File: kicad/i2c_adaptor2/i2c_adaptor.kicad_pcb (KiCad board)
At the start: 2 copper layers, 16 parts, among them J1 Conn_01x02, J2 Conn_01x05, J3 Conn_01x03, J4 Conn_01x14, J5 Conn_01x02, J6 Conn_01x14, Q1 Fairchild BS170, Q2 Fairchild BS170, SW1 SW_SPDT, U1 pic16f18326

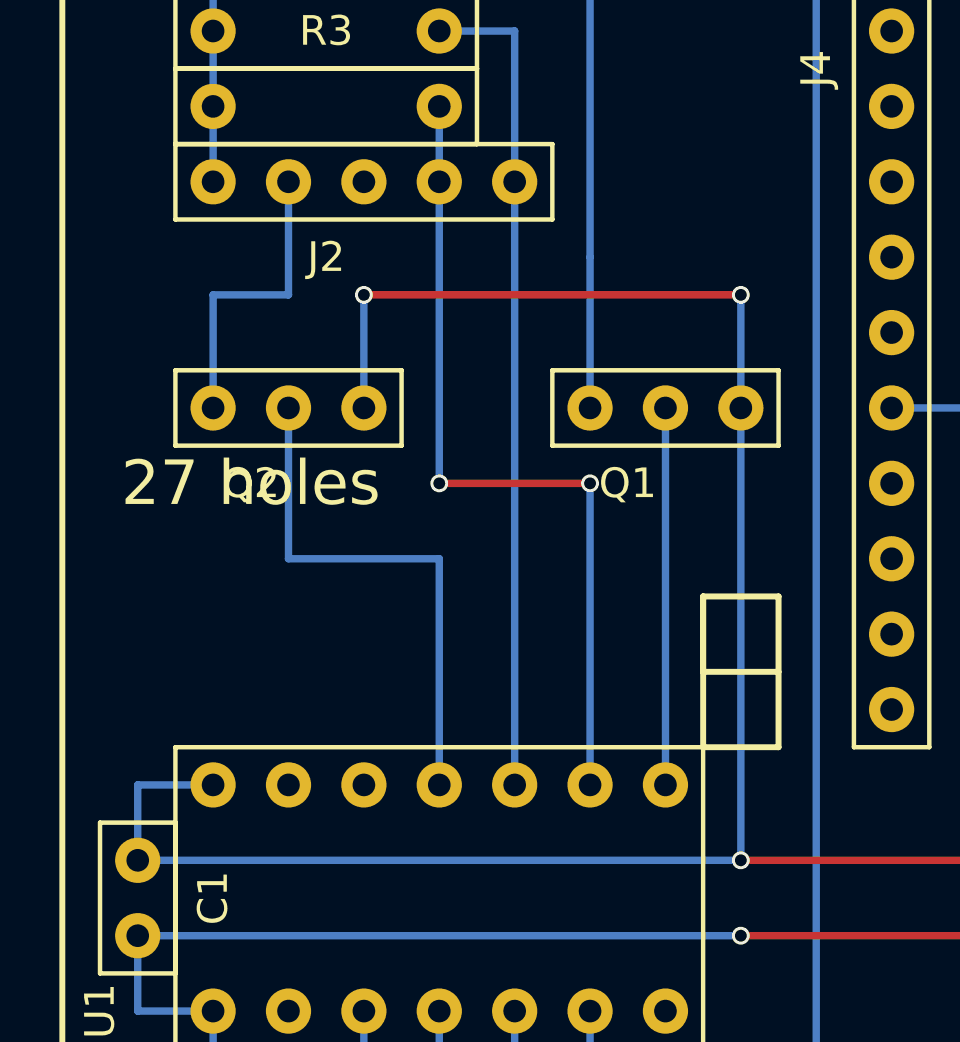
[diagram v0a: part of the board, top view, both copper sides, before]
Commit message: schematic update
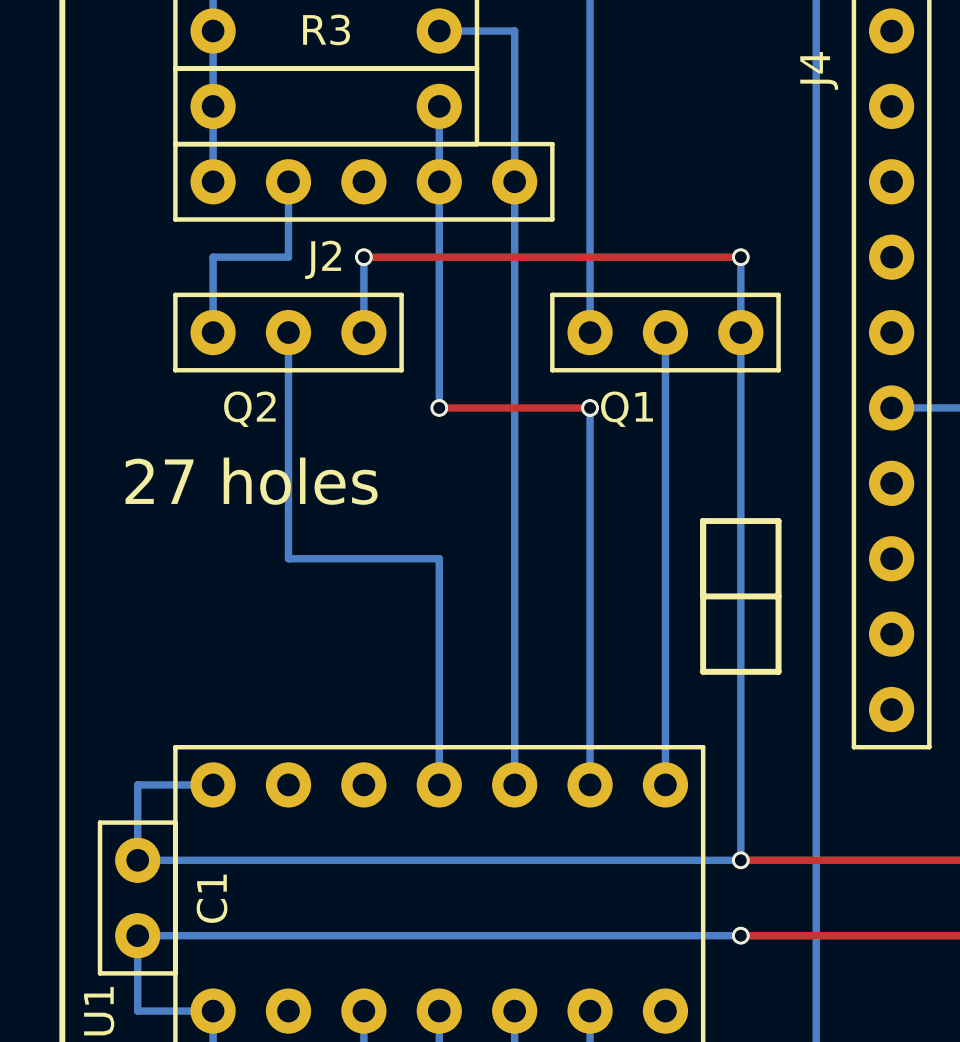
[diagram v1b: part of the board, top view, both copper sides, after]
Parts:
- moved Q1 2.54 mm to (182.9, 102.9)
- moved Q2 2.54 mm to (170.2, 102.9)
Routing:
- net Net-(Q2-Pad2): track 17.8 -> 20.3 mm
- net Net-(Q1-Pad2): track 12.7 -> 15.2 mm
- net FET2: track 10.2 -> 7.62 mm
- net FET1: track 33.0 -> 30.5 mm
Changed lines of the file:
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@@
     (links 34)
     (no_connects 0)
-    (area 0 0 0 0)
+    (area 161.585 72.289999 209.355 144.585)
     (thickness 1.6)
     (drawings 51)
@@
   )
   (module pic16f1:BS170 (layer F.Cu)
-    (at 182.88 105.41)
+    (at 182.88 102.87)
     (fp_text reference Q1 (at -1.27 2.54) (layer F.SilkS)
       (effects (font (size 1 1) (thickness 0.15)))
@@
   )
   (module pic16f1:BS170 (layer F.Cu)
-    (at 170.18 105.41)
+    (at 170.18 102.87)
     (fp_text reference Q2 (at -1.27 2.54) (layer F.SilkS)
       (effects (font (size 1 1) (thickness 0.15)))
@@
   )
   (gr_line (start 184.15 114.3) (end 186.69 114.3) (angle 90) (layer F.SilkS) (width 0.2))
-  (gr_line (start 184.15 111.76) (end 184.15 114.3) (angle 90) (layer F.SilkS) (width 0.2))
+  (gr_line (start 184.15 109.22) (end 184.15 111.76) (angle 90) (layer F.SilkS) (width 0.2))
   (gr_line (start 186.69 111.76) (end 184.15 111.76) (angle 90) (layer F.SilkS) (width 0.2))
-  (gr_line (start 186.69 116.84) (end 186.69 111.76) (angle 90) (layer F.SilkS) (width 0.2))
-  (gr_line (start 184.15 116.84) (end 186.69 116.84) (angle 90) (layer F.SilkS) (width 0.2))
-  (gr_line (start 184.15 111.76) (end 184.15 116.84) (angle 90) (layer F.SilkS) (width 0.2))
+  (gr_line (start 186.69 114.3) (end 186.69 109.22) (angle 90) (layer F.SilkS) (width 0.2))
+  (gr_line (start 184.15 109.22) (end 186.69 109.22) (angle 90) (layer F.SilkS) (width 0.2))
+  (gr_line (start 184.15 109.22) (end 184.15 114.3) (angle 90) (layer F.SilkS) (width 0.2))
   (gr_line (start 168.91 134.62) (end 168.91 132.08) (angle 90) (layer B.Paste) (width 0.2))
   (gr_line (start 171.45 134.62) (end 171.45 132.08) (angle 90) (layer B.Paste) (width 0.2))
@@
   (segment (start 167.64 97.79) (end 167.64 95.25) (width 0.25) (layer B.Cu) (net 1) (status 10))
   (segment (start 167.64 128.27) (end 167.64 125.73) (width 0.25) (layer B.Cu) (net 1) (status 10))
-  (segment (start 185.42 105.41) (end 185.42 101.6) (width 0.25) (layer B.Cu) (net 2))
-  (segment (start 172.72 101.6) (end 172.72 105.41) (width 0.25) (layer B.Cu) (net 2))
-  (via (at 172.72 101.6) (size 0.6) (drill 0.4) (layers F.Cu B.Cu) (net 2))
-  (segment (start 185.42 101.6) (end 172.72 101.6) (width 0.25) (layer F.Cu) (net 2))
-  (via (at 185.42 101.6) (size 0.6) (drill 0.4) (layers F.Cu B.Cu) (net 2))
+  (segment (start 185.42 102.87) (end 185.42 100.33) (width 0.25) (layer B.Cu) (net 2) (status 10))
+  (segment (start 172.72 100.33) (end 172.72 102.87) (width 0.25) (layer B.Cu) (net 2) (status 20))
+  (via (at 172.72 100.33) (size 0.6) (drill 0.4) (layers F.Cu B.Cu) (net 2))
+  (segment (start 185.42 100.33) (end 172.72 100.33) (width 0.25) (layer F.Cu) (net 2))
+  (via (at 185.42 100.33) (size 0.6) (drill 0.4) (layers F.Cu B.Cu) (net 2))
   (segment (start 195.58 120.65) (end 195.58 133.35) (width 0.25) (layer B.Cu) (net 2))
   (segment (start 195.58 133.35) (end 195.58 125.73) (width 0.25) (layer B.Cu) (net 2) (status 20))
   (segment (start 185.42 120.65) (end 195.58 120.65) (width 0.25) (layer F.Cu) (net 2))
-  (segment (start 185.42 120.65) (end 185.42 105.41) (width 0.25) (layer B.Cu) (net 2) (status 20))
+  (segment (start 185.42 120.65) (end 185.42 102.87) (width 0.25) (layer B.Cu) (net 2) (status 20))
   (segment (start 165.1 120.65) (end 185.42 120.65) (width 0.25) (layer B.Cu) (net 2))
   (via (at 185.42 120.65) (size 0.6) (drill 0.4) (layers F.Cu B.Cu) (net 2))
@@
   (segment (start 180.34 140.97) (end 185.42 140.97) (width 0.25) (layer B.Cu) (net 4))
   (segment (start 175.26 95.25) (end 175.26 97.79) (width 0.25) (layer B.Cu) (net 6) (status 20))
-  (segment (start 175.26 97.79) (end 175.26 107.95) (width 0.25) (layer B.Cu) (net 6) (status 10))
-  (segment (start 180.34 107.95) (end 180.34 118.11) (width 0.25) (layer B.Cu) (net 6) (status 20))
-  (via (at 180.34 107.95) (size 0.6) (drill 0.4) (layers F.Cu B.Cu) (net 6))
-  (segment (start 175.26 107.95) (end 180.34 107.95) (width 0.25) (layer F.Cu) (net 6))
-  (via (at 175.26 107.95) (size 0.6) (drill 0.4) (layers F.Cu B.Cu) (net 6))
+  (segment (start 175.26 97.79) (end 175.26 105.41) (width 0.25) (layer B.Cu) (net 6) (status 400010))
+  (segment (start 180.34 105.41) (end 180.34 118.11) (width 0.25) (layer B.Cu) (net 6) (status 800020))
+  (via (at 180.34 105.41) (size 0.6) (drill 0.4) (layers F.Cu B.Cu) (net 6))
+  (segment (start 175.26 105.41) (end 180.34 105.41) (width 0.25) (layer F.Cu) (net 6))
+  (via (at 175.26 105.41) (size 0.6) (drill 0.4) (layers F.Cu B.Cu) (net 6))
   (segment (start 175.26 92.71) (end 177.8 92.71) (width 0.25) (layer B.Cu) (net 7) (status 10))
   (segment (start 177.8 92.71) (end 177.8 97.79) (width 0.25) (layer B.Cu) (net 7) (status 20))
@@
   (segment (start 193.04 105.41) (end 190.5 105.41) (width 0.25) (layer B.Cu) (net 16))
   (segment (start 175.26 128.27) (end 175.26 125.73) (width 0.25) (layer B.Cu) (net 30) (status 10))
-  (segment (start 182.88 118.11) (end 182.88 105.41) (width 0.25) (layer B.Cu) (net 36) (status 20))
-  (segment (start 182.88 105.41) (end 182.88 105.41) (width 0.25) (layer B.Cu) (net 36) (status 30))
+  (segment (start 182.88 118.11) (end 182.88 102.87) (width 0.25) (layer B.Cu) (net 36) (status 20))
+  (segment (start 182.88 102.87) (end 182.88 102.87) (width 0.25) (layer B.Cu) (net 36) (status 30))
   (segment (start 175.26 130.81) (end 175.26 133.35) (width 0.25) (layer B.Cu) (net 37) (status 10))
   (segment (start 172.72 125.73) (end 172.72 130.81) (width 0.25) (layer B.Cu) (net 37) (status 20))
   (segment (start 172.72 130.81) (end 175.26 130.81) (width 0.25) (layer B.Cu) (net 37) (status 30))
-  (segment (start 167.64 105.41) (end 167.64 101.6) (width 0.25) (layer B.Cu) (net 38))
-  (segment (start 170.18 101.6) (end 170.18 97.79) (width 0.25) (layer B.Cu) (net 38))
-  (segment (start 167.64 101.6) (end 170.18 101.6) (width 0.25) (layer B.Cu) (net 38))
+  (segment (start 167.64 102.87) (end 167.64 100.33) (width 0.25) (layer B.Cu) (net 38) (status 10))
+  (segment (start 170.18 100.33) (end 170.18 97.79) (width 0.25) (layer B.Cu) (net 38))
+  (segment (start 167.64 100.33) (end 170.18 100.33) (width 0.25) (layer B.Cu) (net 38))
   (segment (start 182.88 82.55) (end 180.34 82.55) (width 0.25) (layer B.Cu) (net 39))
   (segment (start 190.5 82.55) (end 182.88 82.55) (width 0.25) (layer B.Cu) (net 39))
   (segment (start 180.34 82.55) (end 180.34 100.33) (width 0.25) (layer B.Cu) (net 39))
-  (segment (start 180.34 105.41) (end 180.34 100.33) (width 0.25) (layer B.Cu) (net 39) (status 10))
-  (segment (start 170.18 105.41) (end 170.18 110.49) (width 0.25) (layer B.Cu) (net 40))
+  (segment (start 180.34 102.87) (end 180.34 100.33) (width 0.25) (layer B.Cu) (net 39) (status 10))
+  (segment (start 170.18 102.87) (end 170.18 110.49) (width 0.25) (layer B.Cu) (net 40) (status 10))
   (segment (start 175.26 110.49) (end 175.26 118.11) (width 0.25) (layer B.Cu) (net 40))
   (segment (start 170.18 110.49) (end 175.26 110.49) (width 0.25) (layer B.Cu) (net 40))
